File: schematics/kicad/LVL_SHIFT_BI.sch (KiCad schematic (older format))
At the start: 18 parts

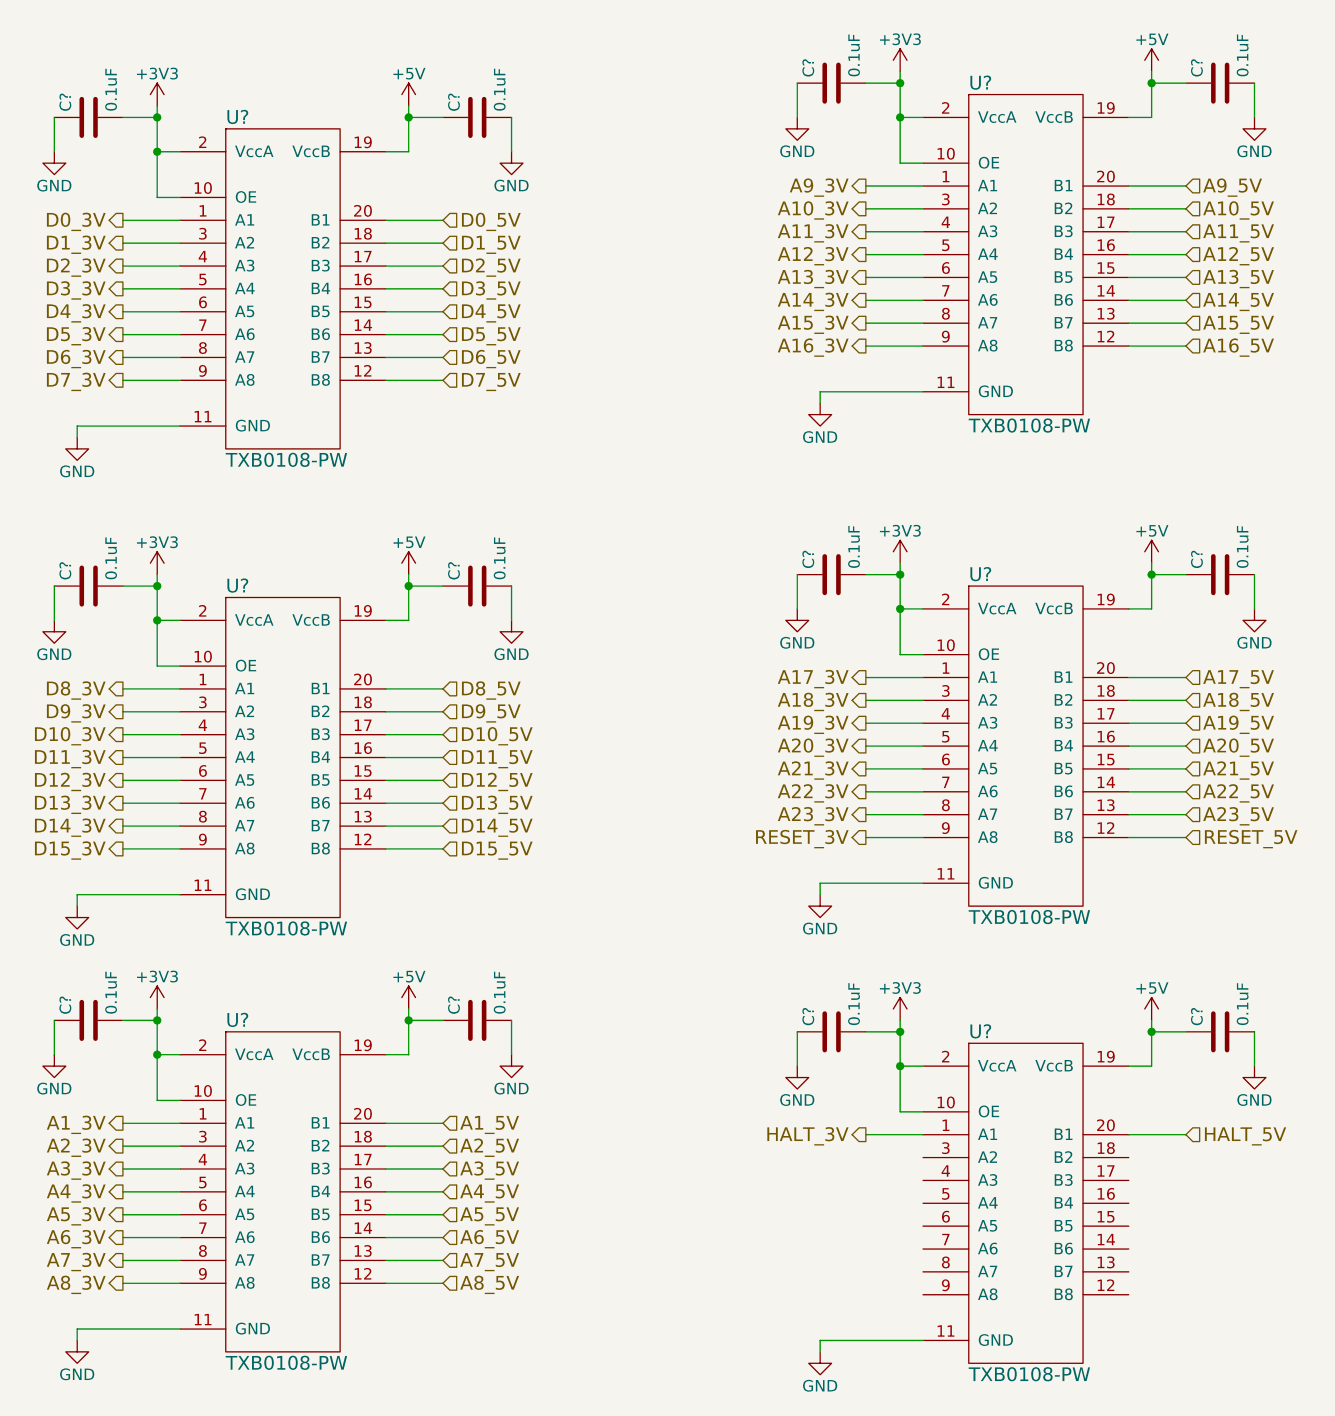
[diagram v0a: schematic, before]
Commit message: Change a lot of things, especially pinning between sheets
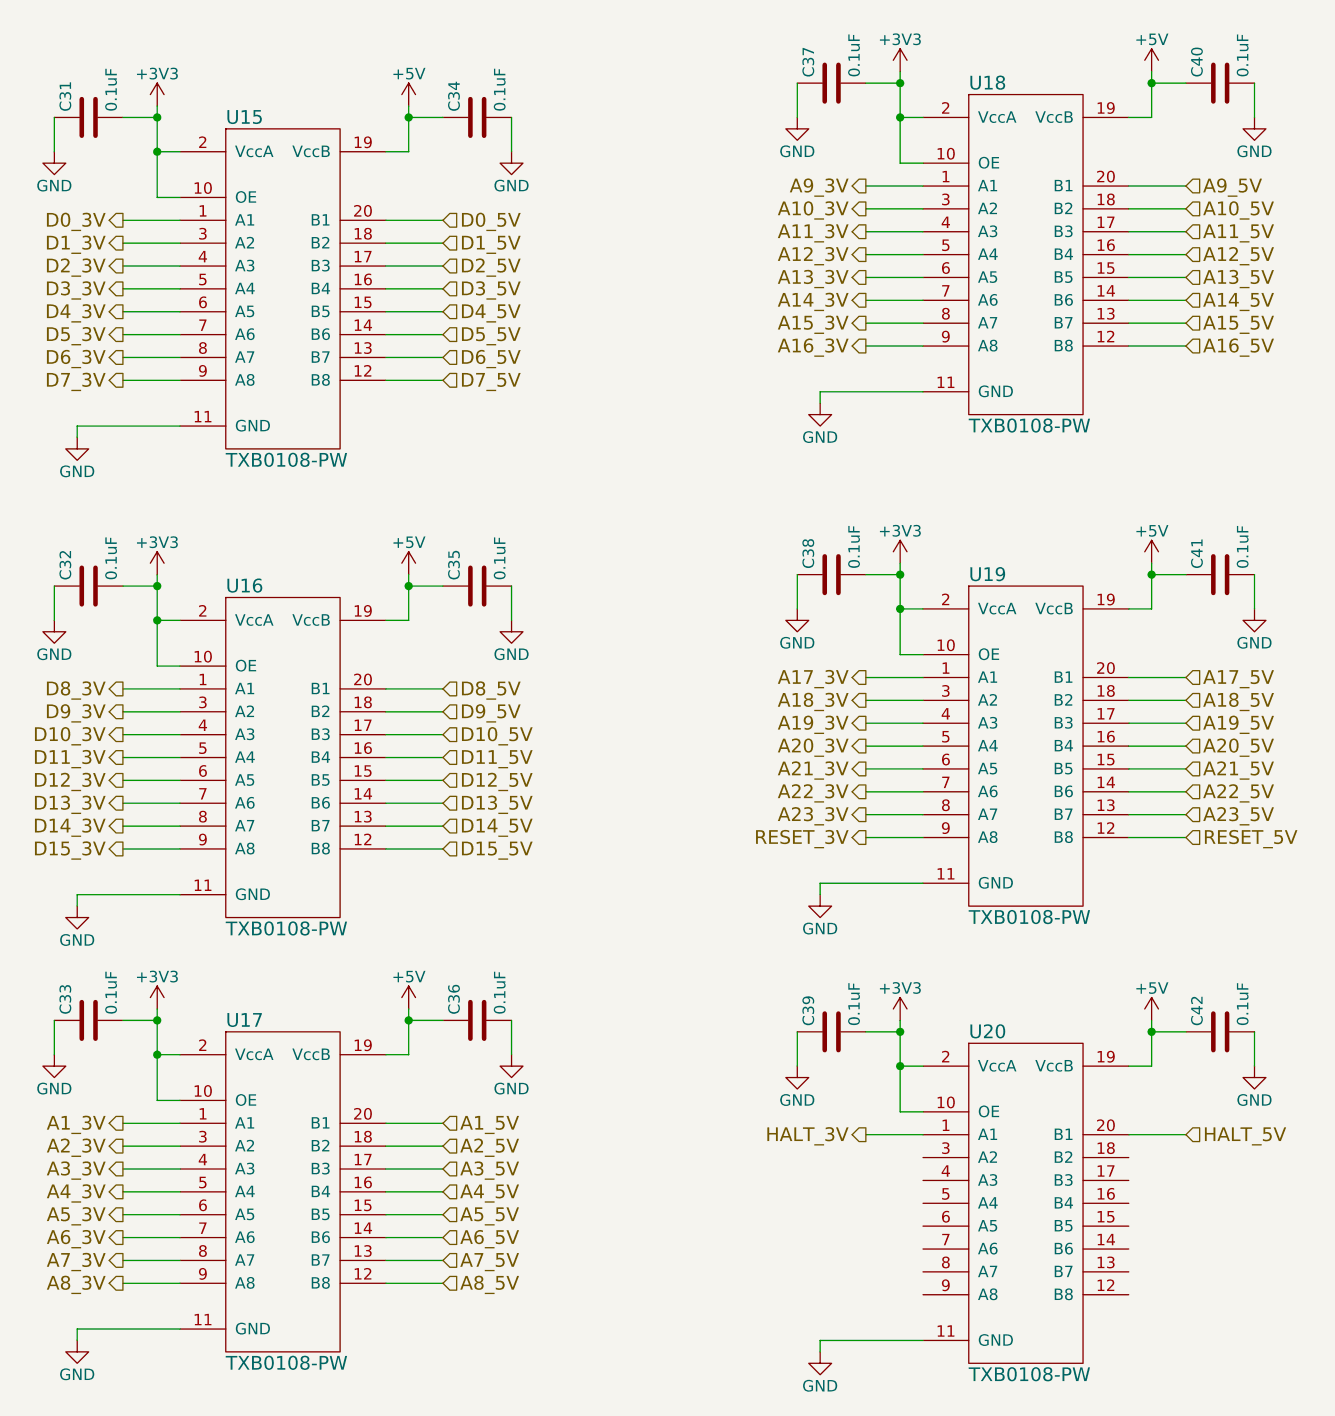
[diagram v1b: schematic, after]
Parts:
- gave numbers to parts that had none: 18
